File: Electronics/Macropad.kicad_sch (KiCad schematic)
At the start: 45 parts, among them SW1 CherryMX, SW10 CherryMX, SW11 CherryMX, SW12 CherryMX, SW13 CherryMX, SW14 CherryMX, SW15 CherryMX, SW16 CherryMX, SW17 CherryMX, SW18 CherryMX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

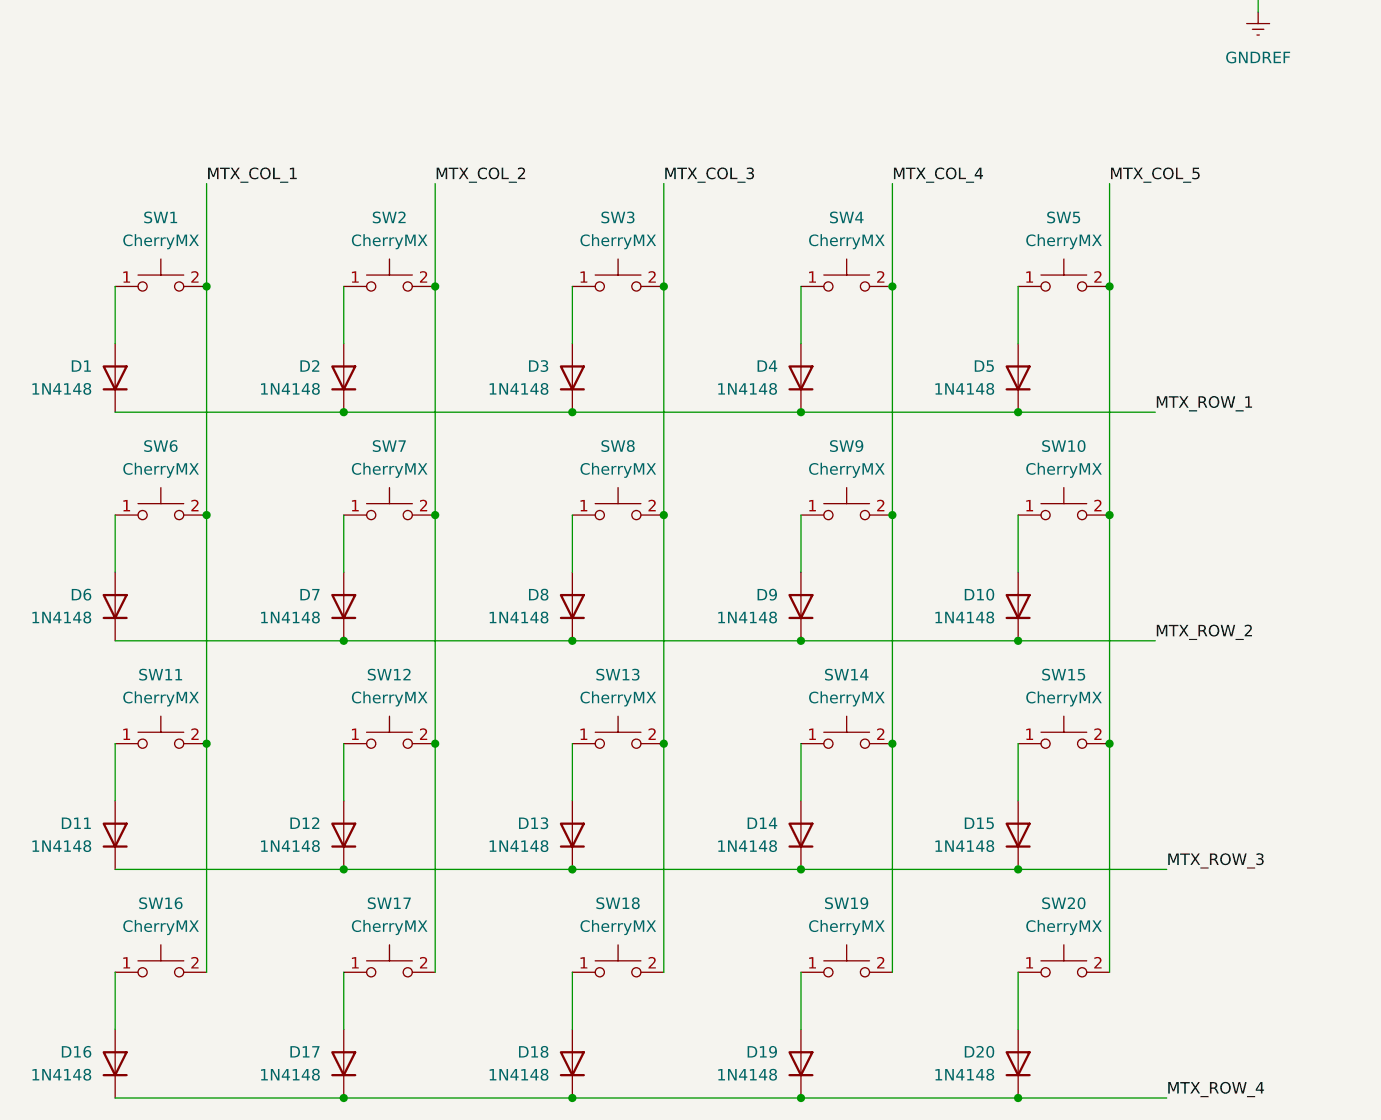
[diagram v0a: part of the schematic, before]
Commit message: Removed Gerbers, fixed row/column diode inversion
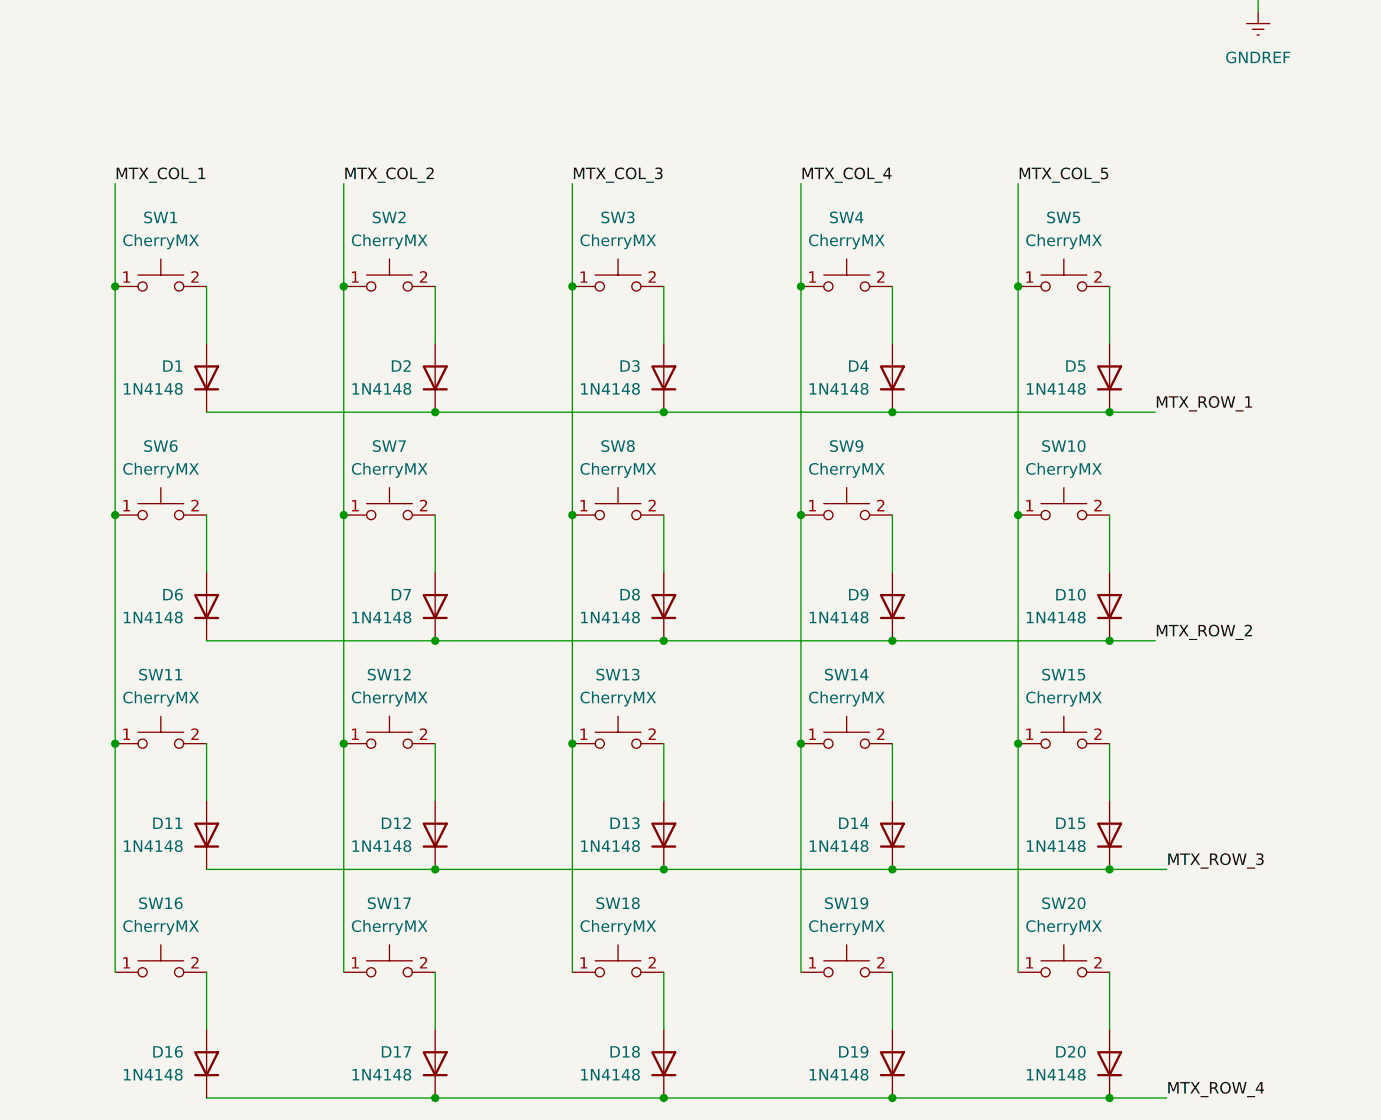
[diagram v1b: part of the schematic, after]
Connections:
- net MTX_COL_1: now also SW1.1, SW11.1, SW16.1, SW6.1; no longer SW1.2, SW11.2, SW16.2, SW6.2
- net MTX_COL_2: now also SW12.1, SW17.1, SW2.1, SW7.1; no longer SW12.2, SW17.2, SW2.2, SW7.2
- net MTX_COL_3: now also SW13.1, SW18.1, SW3.1, SW8.1; no longer SW13.2, SW18.2, SW3.2, SW8.2
- net MTX_COL_4: now also SW14.1, SW19.1, SW4.1, SW9.1; no longer SW14.2, SW19.2, SW4.2, SW9.2
- net MTX_COL_5: now also SW10.1, SW15.1, SW20.1, SW5.1; no longer SW10.2, SW15.2, SW20.2, SW5.2
- net at D1.2 (A): now also SW1.2; no longer SW1.1
- net at D17.2 (A): now also SW17.2; no longer SW17.1
- net at D13.2 (A): now also SW13.2; no longer SW13.1
- net at D4.2 (A): now also SW4.2; no longer SW4.1
- net at D3.2 (A): now also SW3.2; no longer SW3.1
- net at D12.2 (A): now also SW12.2; no longer SW12.1
- net at D11.2 (A): now also SW11.2; no longer SW11.1
- net at D5.2 (A): now also SW5.2; no longer SW5.1
- net at D20.2 (A): now also SW20.2; no longer SW20.1
- net at D6.2 (A): now also SW6.2; no longer SW6.1
- net at D7.2 (A): now also SW7.2; no longer SW7.1
- net at D10.2 (A): now also SW10.2; no longer SW10.1
- net at D8.2 (A): now also SW8.2; no longer SW8.1
- net at D14.2 (A): now also SW14.2; no longer SW14.1
- net at D15.2 (A): now also SW15.2; no longer SW15.1
- net at D2.2 (A): now also SW2.2; no longer SW2.1
- net at D19.2 (A): now also SW19.2; no longer SW19.1
- net at D18.2 (A): now also SW18.2; no longer SW18.1
- net at D16.2 (A): now also SW16.2; no longer SW16.1
- net at D9.2 (A): now also SW9.2; no longer SW9.1
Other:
- moved on the sheet: D1, D10, D11, D12, D13, D14, D15, D16, D17, D18, D19, D2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
